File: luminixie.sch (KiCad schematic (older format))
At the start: 27 parts, among them J1 Conn_01x03_Female, U1 ESP32-MINIKIT, U2 HV-POWER, U3 HV5530_PLCC, U4 HV5530_PLCC

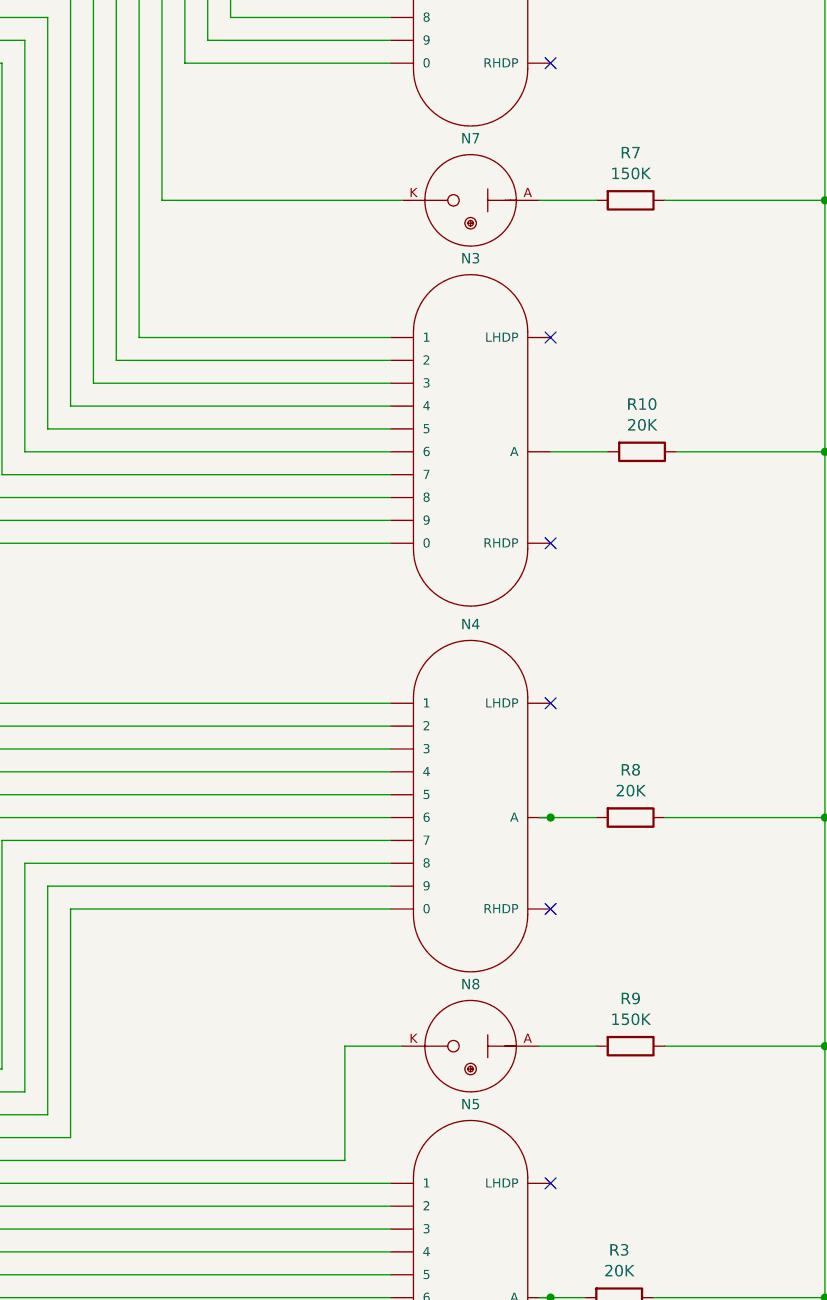
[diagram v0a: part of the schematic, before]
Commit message: Voltage divider for IN-3
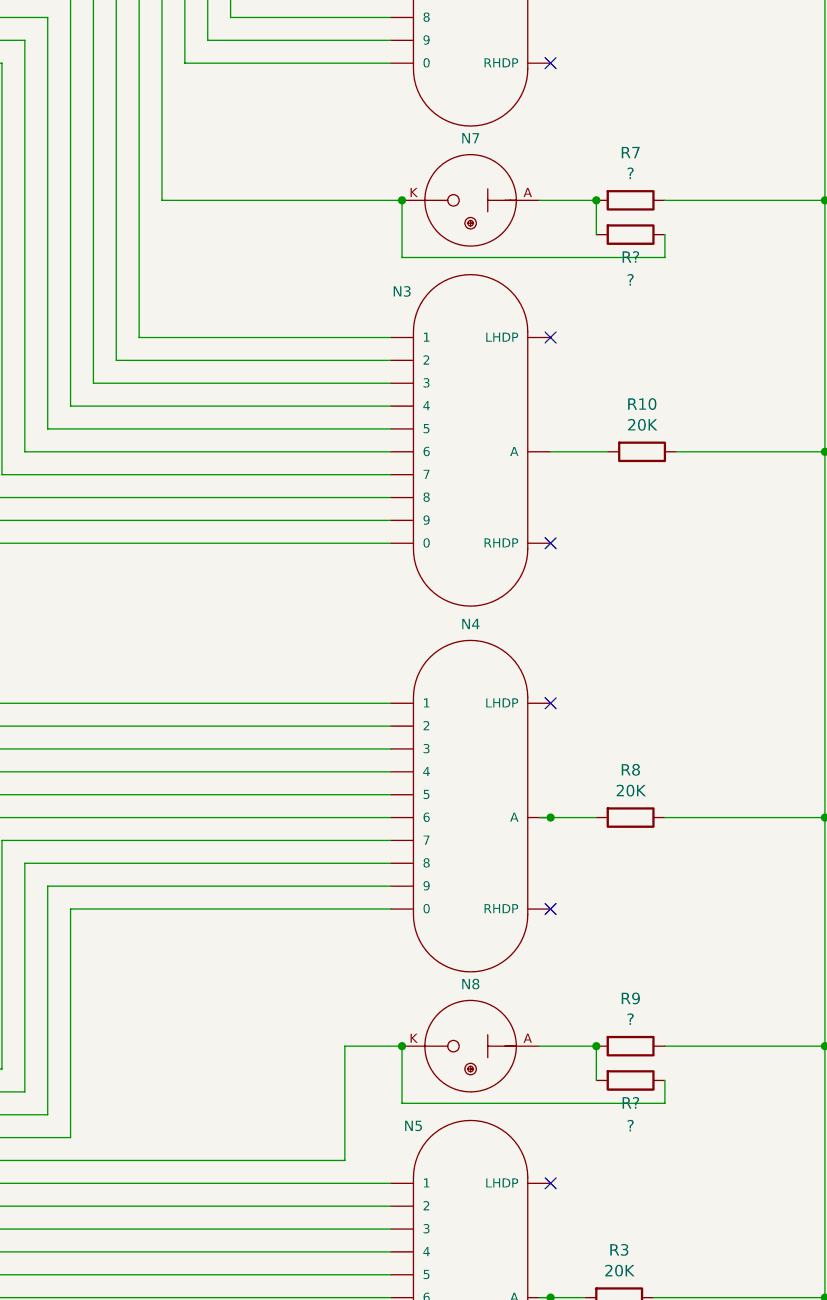
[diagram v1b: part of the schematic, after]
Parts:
- added R? (x2): ?, Resistor_THT:R_Axial_DIN0207_L6.3mm_D2.5mm_P7.62mm_Horizontal, symbol Device:R
- R7, R9: value 150K -> ?
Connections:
- net at N7.K, U3.6 (HV21): now also R?.1
- net at N8.K, U4.40 (HV11): now also R?.1
- net at N8.A, R9.2: now also R?.2
- net at N7.A, R7.2: now also R?.2
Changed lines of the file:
@@
 Wire Wire Line
 	6750 5250 6750 3950
-Wire Wire Line
-	7800 5250 6750 5250
 Connection ~ 9650 4250
 Wire Wire Line
@@
 U 1 1 5D625495
 P 8050 9950
-F 0 "N5" H 8100 10695 45  0000 C CNN
+F 0 "N5" H 7850 10600 45  0000 C CNN
 F 1 "IN-14" H 8050 9950 45  0001 L BNN
 F 2 "nixies-us:nixies-us-IN-14" H 8080 10100 20  0001 C CNN
@@
 U 1 1 5D62345B
 P 8050 6250
-F 0 "N3" H 8100 6995 45  0000 C CNN
+F 0 "N3" H 7800 6850 45  0000 C CNN
 F 1 "IN-14" H 8050 6250 45  0001 L BNN
 F 2 "nixies-us:nixies-us-IN-14" H 8080 6400 20  0001 C CNN
@@
 	-1   0    0    1
 $EndComp
-$Comp
-L Device:R R7
-U 1 1 5D64372C
-P 8800 5250
-F 0 "R7" V 8593 5250 50  0000 C CNN
-F 1 "150K" V 8684 5250 50  0000 C CNN
-F 2 "Resistor_THT:R_Axial_DIN0207_L6.3mm_D2.5mm_P7.62mm_Horizontal" V 8730 5250 50  0001 C CNN
-F 3 "~" H 8800 5250 50  0001 C CNN
-	1    8800 5250
-	0    1    1    0
-$EndComp
 Wire Wire Line
 	8400 5250 8650 5250
@@
 P 8800 8950
 F 0 "R9" V 8593 8950 50  0000 C CNN
-F 1 "150K" V 8684 8950 50  0000 C CNN
+F 1 "?" V 8684 8950 50  0000 C CNN
 F 2 "Resistor_THT:R_Axial_DIN0207_L6.3mm_D2.5mm_P7.62mm_Horizontal" V 8730 8950 50  0001 C CNN
 F 3 "~" H 8800 8950 50  0001 C CNN
@@
 Wire Wire Line
 	3700 1450 9650 1450
-Wire Wire Line
-	7550 8950 7800 8950
 NoConn ~ 5450 11700
 NoConn ~ 5450 11550
@@
 	10550 7050 10550 7400
 NoConn ~ 9950 7600
+Wire Wire Line
+	8650 5250 8650 5400
+Connection ~ 8650 5250
+Wire Wire Line
+	8950 5400 8950 5500
+Wire Wire Line
+	8950 5500 7800 5500
+$Comp
+L Device:R R7
+U 1 1 5D64372C
+P 8800 5250
+F 0 "R7" V 8593 5250 50  0000 C CNN
+F 1 "?" V 8684 5250 50  0000 C CNN
+F 2 "Resistor_THT:R_Axial_DIN0207_L6.3mm_D2.5mm_P7.62mm_Horizontal" V 8730 5250 50  0001 C CNN
+F 3 "~" H 8800 5250 50  0001 C CNN
+	1    8800 5250
+	0    1    1    0
+$EndComp
+$Comp
+L Device:R R?
+U 1 1 5D91AA0C
+P 8800 5400
+F 0 "R?" V 8900 5400 50  0000 C CNN
+F 1 "?" V 9000 5400 50  0000 C CNN
+F 2 "Resistor_THT:R_Axial_DIN0207_L6.3mm_D2.5mm_P7.62mm_Horizontal" V 8730 5400 50  0001 C CNN
+F 3 "~" H 8800 5400 50  0001 C CNN
+	1    8800 5400
+	0    1    1    0
+$EndComp
+$Comp
+L Device:R R?
+U 1 1 5D935C0E
+P 8800 9100
+F 0 "R?" V 8900 9100 50  0000 C CNN
+F 1 "?" V 9000 9100 50  0000 C CNN
+F 2 "Resistor_THT:R_Axial_DIN0207_L6.3mm_D2.5mm_P7.62mm_Horizontal" V 8730 9100 50  0001 C CNN
+F 3 "~" H 8800 9100 50  0001 C CNN
+	1    8800 9100
+	0    1    1    0
+$EndComp
+Wire Wire Line
+	8650 9100 8650 8950
+Connection ~ 8650 8950
+Wire Wire Line
+	8950 9100 8950 9200
+Wire Wire Line
+	8950 9200 7800 9200
+Wire Wire Line
+	7800 5250 7800 5500
+Connection ~ 7800 5250
+Wire Wire Line
+	6750 5250 7800 5250
+Wire Wire Line
+	7800 8950 7800 9200
+Connection ~ 7800 8950
+Wire Wire Line
+	7550 8950 7800 8950
 $EndSCHEMATC
